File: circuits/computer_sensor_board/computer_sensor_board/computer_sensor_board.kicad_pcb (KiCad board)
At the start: 2 copper layers, 50 x 35 mm, 7 parts, among them J2 Conn_Jetson, J5 Conn_VLP16, J6 Conn_Main_DCDC, J7 Conn_Router

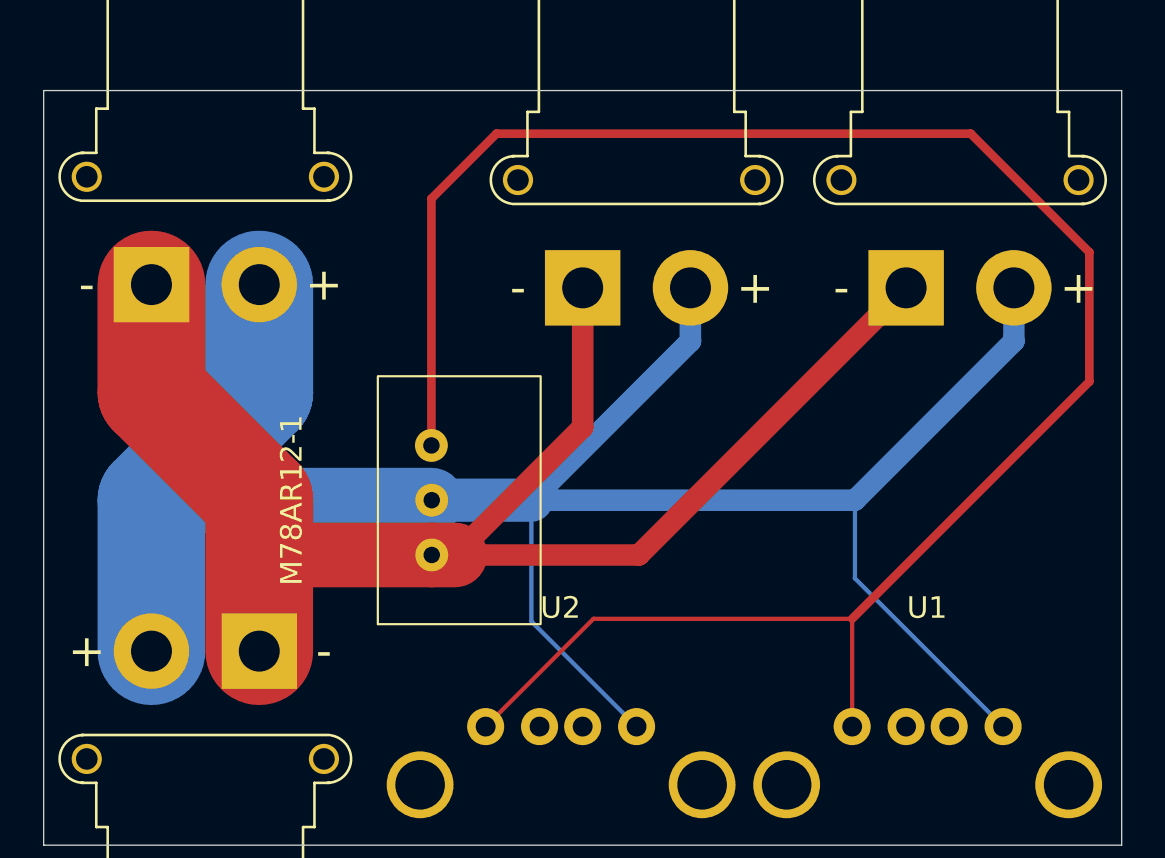
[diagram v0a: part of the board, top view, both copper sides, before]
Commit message: add M78AR05 ad converter
Signed-off-by: Masaya Kataoka <ms.kataoka@gmail.com>
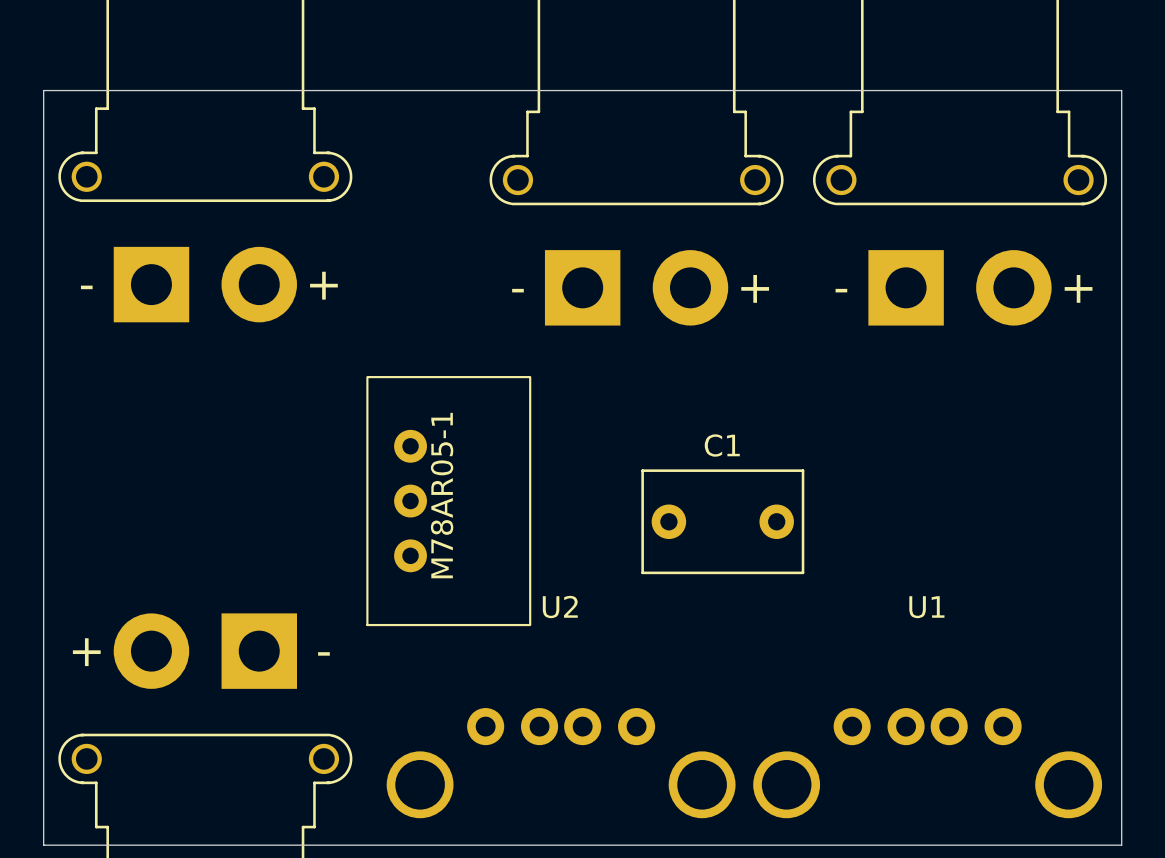
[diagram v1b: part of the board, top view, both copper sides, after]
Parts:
- removed M78AR12-1: ~, M78AR15:M78AR15
- added C1: 3.3uF, Capacitor_THT:C_Rect_L7.2mm_W4.5mm_P5.00mm_FKS2_FKP2_MKS2_MKP2, F.Cu at (209.0, 75.0)
- added M78AR05-1: ~, M78AR05-1:M78AR05-1, F.Cu at (199.0, 73.8)
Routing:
- net Net-(J2-Pin_2): track 108.0 -> 0.00 mm
- net Net-(M78AR05-1-Vout): track 91.1 -> 0.00 mm
- net Net-(J2-Pin_1): track 71.8 -> 0.00 mm

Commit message: update design
Signed-off-by: Masaya Kataoka <ms.kataoka@gmail.com>
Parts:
- moved C1 3.81 mm to (207.5, 71.5), turned to -90 degrees
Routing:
- net Net-(J2-Pin_2): track 0.00 -> 94.1 mm
- net Net-(J2-Pin_1): track 0.00 -> 77.8 mm
- net Net-(M78AR05-1-Vout): track 0.00 -> 42.7 mm

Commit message: add mounting hole
Signed-off-by: Masaya Kataoka <ms.kataoka@gmail.com>
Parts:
- added H1: MountingHole, MountingHole:MountingHole_3.2mm_M3, F.Cu at (175.0, 60.0)
- added H2: MountingHole, MountingHole:MountingHole_3.2mm_M3, F.Cu at (235.0, 60.0)
- added H3: MountingHole, MountingHole:MountingHole_3.2mm_M3, F.Cu at (175.0, 85.0)
- added H4: MountingHole, MountingHole:MountingHole_3.2mm_M3, F.Cu at (235.0, 85.0)
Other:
- board size 50 x 35 mm -> 70 x 35 mm

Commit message: enable generate gerber
Signed-off-by: Masaya Kataoka <ms.kataoka@gmail.com>
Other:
- rule pad_to_mask_clearance: 0 -> 0.1
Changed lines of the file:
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@@
 			(dielectric_constraints no)
 		)
-		(pad_to_mask_clearance 0)
+		(pad_to_mask_clearance 0.1)
 		(allow_soldermask_bridges_in_footprints no)
+		(aux_axis_origin 170 90)
 		(pcbplotparams
 			(layerselection 0x00010fc_ffffffff)

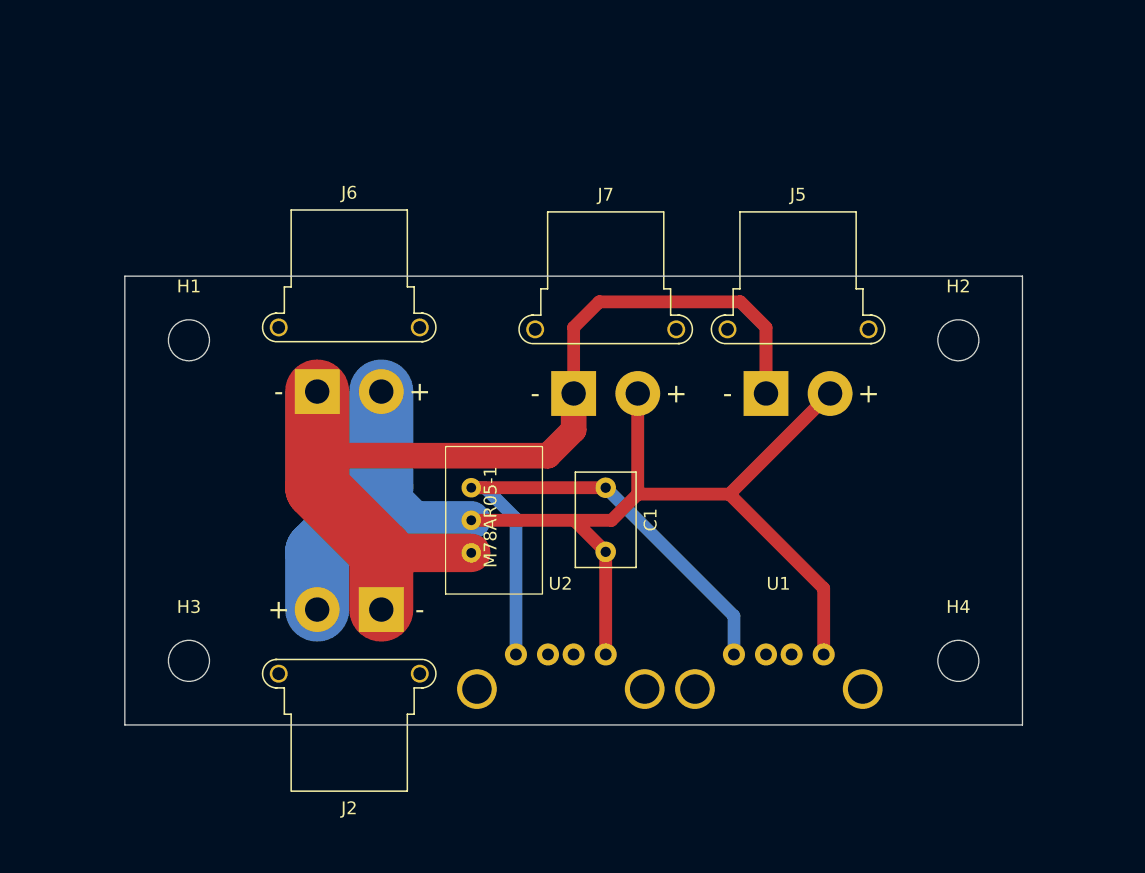
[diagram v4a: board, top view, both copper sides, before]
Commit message: fix board design
Signed-off-by: Masaya Kataoka <ms.kataoka@gmail.com>
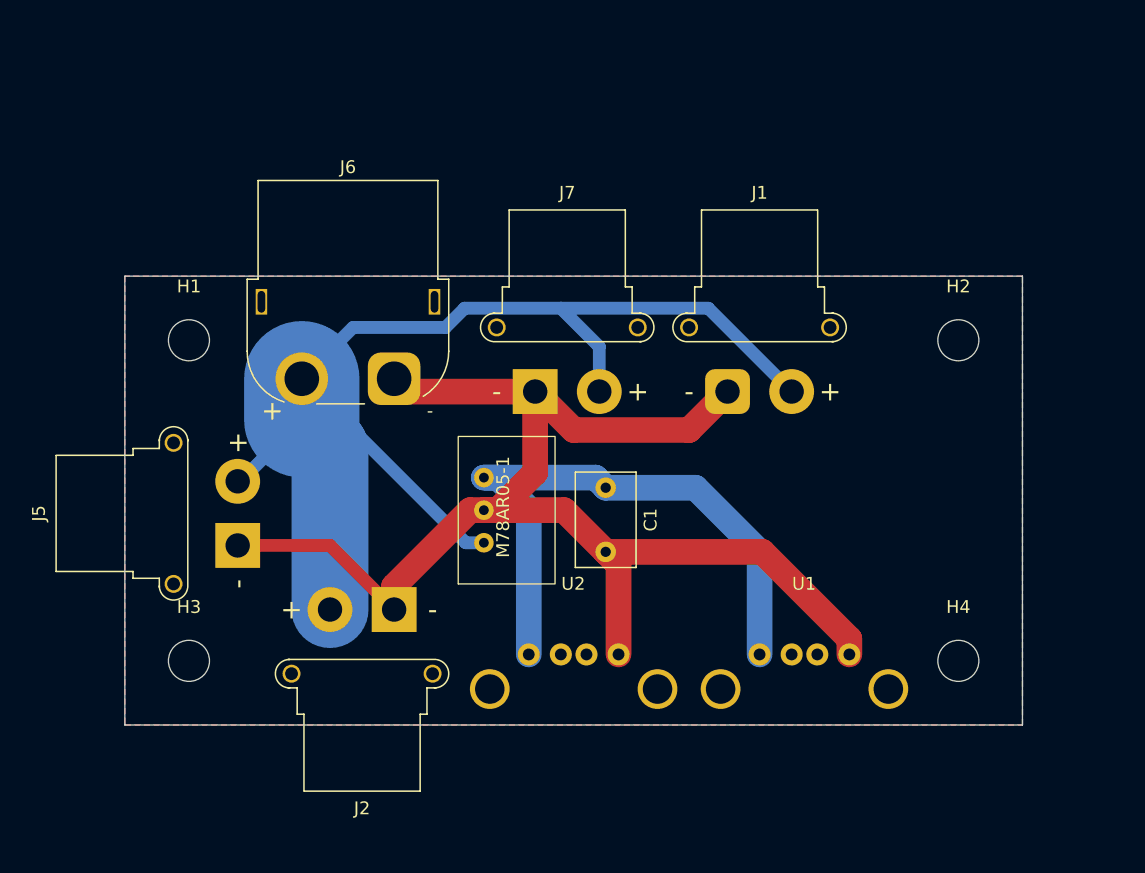
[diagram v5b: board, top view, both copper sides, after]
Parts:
- added J1: Conn_Switching_Hub, Connector_AMASS:AMASS_XT30PW-F_1x02_P2.50mm_Horizontal, F.Cu at (217.0, 64.0)
- J6: footprint Connector_AMASS:AMASS_XT30PW-F_1x02_P2.50mm_Horizontal -> Connector_AMASS:AMASS_XT60PW-F_1x02_P7.20mm_Horizontal
- moved J5 42.9 mm to (178.8, 76.0), turned to 90 degrees
- moved J6 6.08 mm to (191.0, 63.0)
- moved J7 3.00 mm to (202.0, 64.0)
- moved U1 2.00 mm to (223.0, 84.5)
- moved M78AR05-1 1.26 mm to (200.0, 73.0)
- moved J2 1.00 mm to (191.0, 81.0)
- moved U2 1.00 mm to (205.0, 84.5)
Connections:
- C1 pad 2: Net-(J2-Pin_2) -> GND
- J2 pad 1: Net-(J2-Pin_1) -> GND
- J2 pad 2: Net-(J2-Pin_2) -> Net-(J1-Pin_2)
- J5 pad 1: Net-(J2-Pin_1) -> GND
- J5 pad 2: Net-(J2-Pin_2) -> Net-(J1-Pin_2)
- J6 pad 1: Net-(J2-Pin_1) -> GND
- J6 pad 2: Net-(J2-Pin_2) -> Net-(J1-Pin_2)
- J7 pad 1: Net-(J2-Pin_1) -> GND
- J7 pad 2: Net-(J2-Pin_2) -> Net-(J1-Pin_2)
- M78AR05-1 pad 1: Net-(J2-Pin_1) -> Net-(J1-Pin_2)
- M78AR05-1 pad 2: Net-(J2-Pin_2) -> GND
- U1 pad 4: Net-(J2-Pin_2) -> GND
- U2 pad 4: Net-(J2-Pin_2) -> GND
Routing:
- net GND: track 0.00 -> 108.3 mm
- net Net-(J1-Pin_2): track 0.00 -> 96.3 mm
- net Net-(J2-Pin_2): track 94.1 -> 0.00 mm
- net Net-(J2-Pin_1): track 77.8 -> 0.00 mm
- net Net-(M78AR05-1-Vout): track 42.7 -> 47.8 mm
- added copper zone on B.Cu, net GND
- added copper zone on F.Cu, net GND

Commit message: Fix/care invert connection (#378)
* add smart battery board

Signed-off-by: Masaya Kataoka <ms.kataoka@gmail.com>

* fix board design

Signed-off-by: Masaya Kataoka <ms.kataoka@gmail.com>

* change Pch MOSFET

Signed-off-by: Masaya Kataoka <ms.kataoka@gmail.com>

* add heatsink

Signed-off-by: Masaya Kataoka <ms.kataoka@gmail.com>

* remove warning

Signed-off-by: Masaya Kataoka <ms.kataoka@gmail.com>

---------

Signed-off-by: Masaya Kataoka <ms.kataoka@gmail.com>
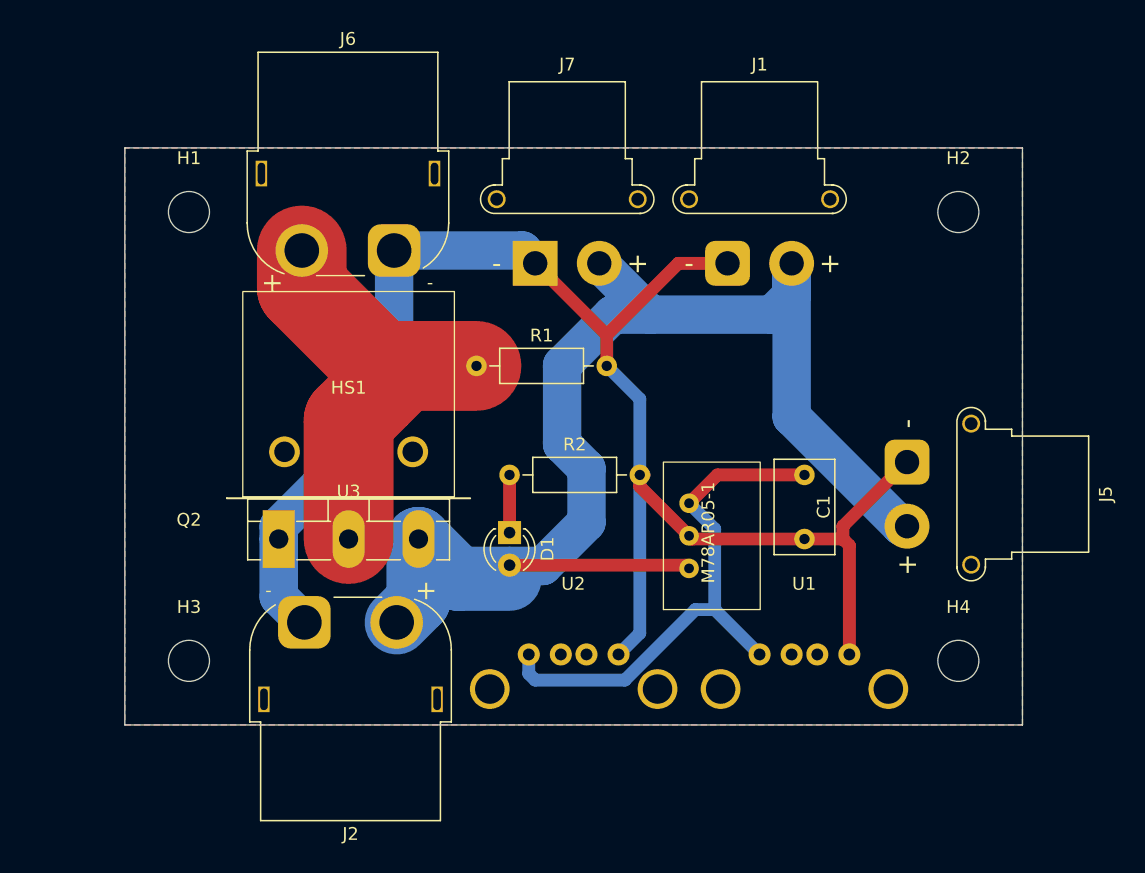
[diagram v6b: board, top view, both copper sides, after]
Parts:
- added D1: LED, LED_THT:LED_D3.0mm, F.Cu at (200.0, 75.0)
- added HS1: Heatsink, 16PB017-01025:16PB017-01025, F.Cu at (187.4, 64.2)
- added Q2: 2SJ555-E, Package_TO_SOT_THT:TO-3P-3_Vertical, F.Cu at (182.0, 75.5)
- added R1: 100K, Resistor_THT:R_Axial_DIN0207_L6.3mm_D2.5mm_P10.16mm_Horizontal, F.Cu at (197.4, 62.0)
- added R2: 390, Resistor_THT:R_Axial_DIN0207_L6.3mm_D2.5mm_P10.16mm_Horizontal, F.Cu at (200.0, 70.5)
- added U3: Heatsink_sheet, 16PB017-01025:TO-3PH, F.Cu at (187.4, 72.3)
- J2: footprint Connector_AMASS:AMASS_XT30PW-F_1x02_P2.50mm_Horizontal -> Connector_AMASS:AMASS_XT60PW-F_1x02_P7.20mm_Horizontal
- moved J5 52.6 mm to (231.0, 69.5), turned to -90 degrees
- moved M78AR05-1 16.1 mm to (216.0, 75.0)
- moved C1 15.5 mm to (223.0, 70.5)
- moved H1 10.0 mm to (175.0, 50.0)
- moved H2 10.0 mm to (235.0, 50.0)
- moved J1 10.0 mm to (217.0, 54.0)
- moved J6 10.0 mm to (191.0, 53.0)
- moved J7 10.0 mm to (202.0, 54.0)
- moved J2 7.07 mm to (184.0, 82.0)
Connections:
- J1 pad 2: Net-(J1-Pin_2) -> Net-(D1-A)
- J2 pad 2: Net-(J1-Pin_2) -> Net-(D1-A)
- J5 pad 2: Net-(J1-Pin_2) -> Net-(D1-A)
- J6 pad 2: Net-(J1-Pin_2) -> Net-(J6-Pin_2)
- J7 pad 2: Net-(J1-Pin_2) -> Net-(D1-A)
- M78AR05-1 pad 1: Net-(J1-Pin_2) -> Net-(D1-A)
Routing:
- net Net-(D1-A): track 0.00 -> 102.9 mm
- net Net-(J1-Pin_2): track 96.3 -> 0.00 mm
- net Net-(J6-Pin_2): track 0.00 -> 34.3 mm
- net GND: track 108.3 -> 127.7 mm
- net Net-(M78AR05-1-Vout): track 47.8 -> 42.5 mm
- net Net-(D1-K): track 0.00 -> 4.50 mm
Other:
- board size 70 x 35 mm -> 70 x 45 mm
